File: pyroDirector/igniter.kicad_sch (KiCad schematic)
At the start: 13 parts, among them J28 LED_ext, J29 Screw_Terminal_01x02, K3 PR12-5V-360-1C, Q12 MMBT2222A 1P, Q13 IRLB8721PbF

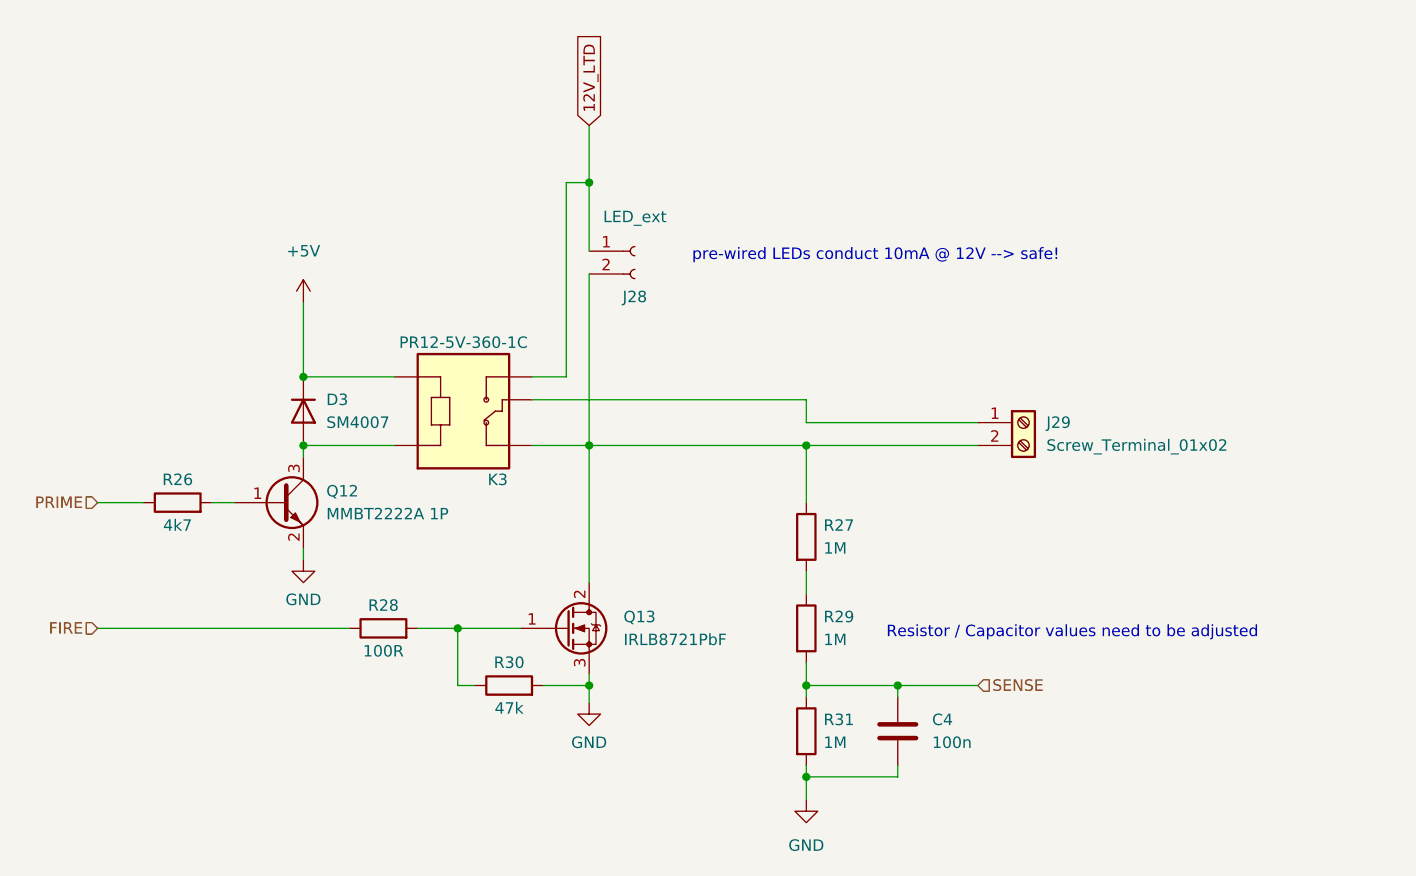
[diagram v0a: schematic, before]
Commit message: Added jacks and PCB switch
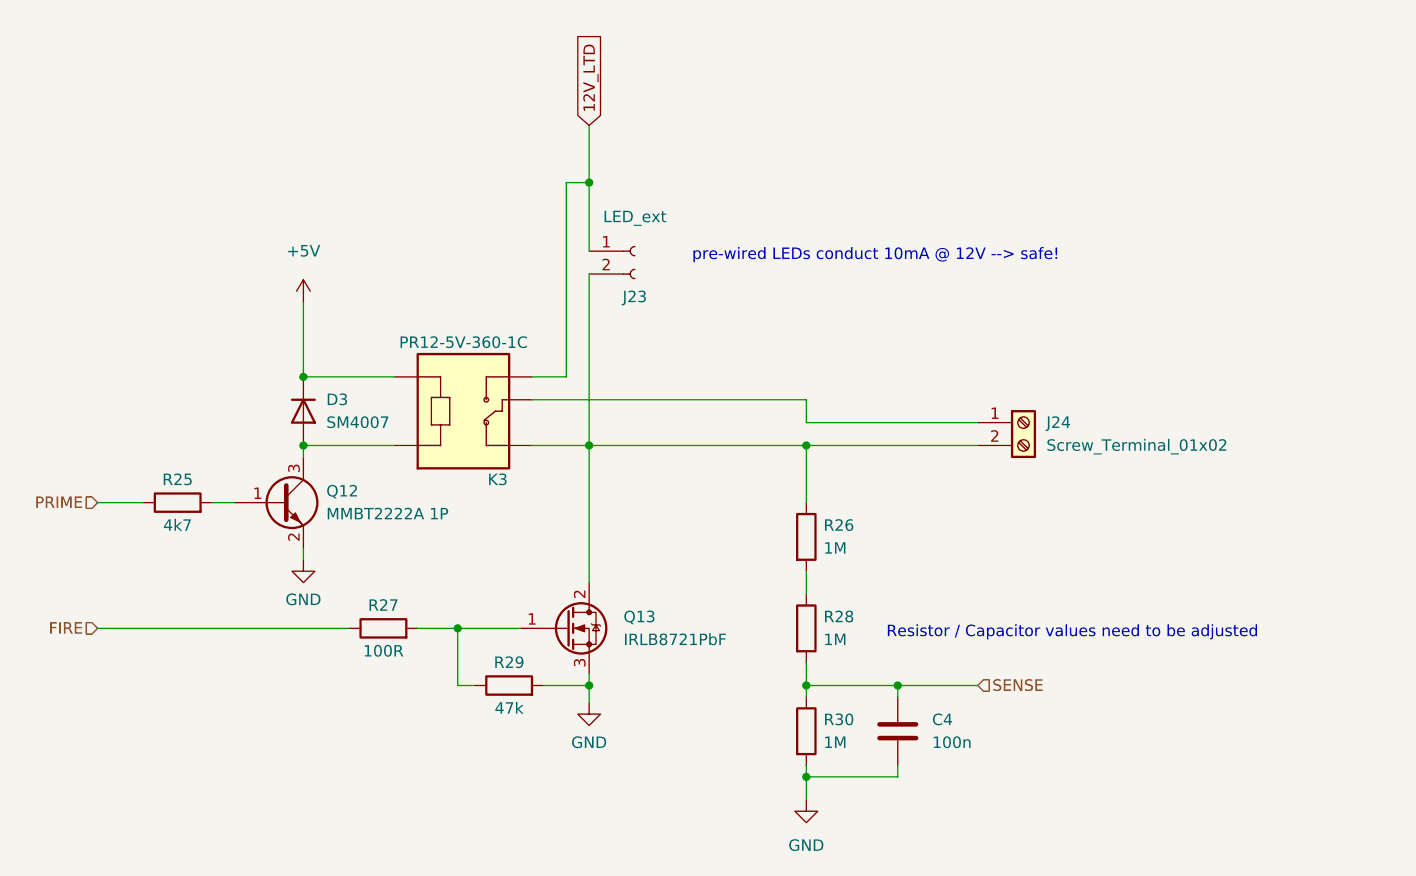
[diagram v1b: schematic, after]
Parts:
- C4: footprint (none) -> Capacitor_SMD:C_0805_2012Metric_Pad1.18x1.45mm_HandSolder
- renumbered J28 to J23, J29 to J24, R26 to R25, R27 to R26, R28 to R27, R29 to R28, R30 to R29, R31 to R30
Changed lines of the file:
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@@
   (symbol (lib_id "power:GND") (at 156.21 130.175 0) (unit 1)
     (in_bom yes) (on_board yes) (fields_autoplaced)
-    (property "Reference" "#PWR043" (id 0) (at 156.21 136.525 0)
+    (property "Reference" "#PWR049" (id 0) (at 156.21 136.525 0)
       (effects (font (size 1.27 1.27)) hide)
     )
@@
   (symbol (lib_id "Device:R") (at 110.49 107.95 90) (unit 1)
     (in_bom yes) (on_board yes)
-    (property "Reference" "R26" (id 0) (at 110.49 105.41 90))
+    (property "Reference" "R25" (id 0) (at 110.49 105.41 90))
     (property "Value" "4k7" (id 1) (at 110.49 110.49 90))
     (property "Footprint" "" (id 2) (at 110.49 109.728 90)
@@
   (symbol (lib_id "Connector:Conn_01x02_Female") (at 161.29 80.01 0) (unit 1)
     (in_bom yes) (on_board yes)
-    (property "Reference" "J28" (id 0) (at 161.29 85.09 0))
+    (property "Reference" "J23" (id 0) (at 161.29 85.09 0))
     (property "Value" "LED_ext" (id 1) (at 161.29 76.2 0))
     (property "Footprint" "" (id 2) (at 161.29 80.01 0)
@@
   (symbol (lib_id "power:GND") (at 180.34 140.97 0) (unit 1)
     (in_bom yes) (on_board yes) (fields_autoplaced)
-    (property "Reference" "#PWR044" (id 0) (at 180.34 147.32 0)
+    (property "Reference" "#PWR050" (id 0) (at 180.34 147.32 0)
       (effects (font (size 1.27 1.27)) hide)
     )
@@
   (symbol (lib_id "Device:R") (at 147.32 128.27 90) (unit 1)
     (in_bom yes) (on_board yes)
-    (property "Reference" "R30" (id 0) (at 147.32 125.73 90))
+    (property "Reference" "R29" (id 0) (at 147.32 125.73 90))
     (property "Value" "47k" (id 1) (at 147.32 130.81 90))
     (property "Footprint" "" (id 2) (at 147.32 130.048 90)
@@
   (symbol (lib_id "power:+5V") (at 124.46 85.725 0) (unit 1)
     (in_bom yes) (on_board yes) (fields_autoplaced)
-    (property "Reference" "#PWR041" (id 0) (at 124.46 89.535 0)
+    (property "Reference" "#PWR047" (id 0) (at 124.46 89.535 0)
       (effects (font (size 1.27 1.27)) hide)
     )
@@
   (symbol (lib_id "Device:R") (at 180.34 121.92 0) (unit 1)
     (in_bom yes) (on_board yes) (fields_autoplaced)
-    (property "Reference" "R29" (id 0) (at 182.245 120.6499 0)
+    (property "Reference" "R28" (id 0) (at 182.245 120.6499 0)
       (effects (font (size 1.27 1.27)) (justify left))
     )
@@
   (symbol (lib_id "Device:R") (at 180.34 133.35 0) (unit 1)
     (in_bom yes) (on_board yes) (fields_autoplaced)
-    (property "Reference" "R31" (id 0) (at 182.245 132.0799 0)
+    (property "Reference" "R30" (id 0) (at 182.245 132.0799 0)
       (effects (font (size 1.27 1.27)) (justify left))
     )
@@
   (symbol (lib_id "Device:R") (at 133.35 121.92 90) (unit 1)
     (in_bom yes) (on_board yes)
-    (property "Reference" "R28" (id 0) (at 133.35 119.38 90))
+    (property "Reference" "R27" (id 0) (at 133.35 119.38 90))
     (property "Value" "100R" (id 1) (at 133.35 124.46 90))
     (property "Footprint" "" (id 2) (at 133.35 123.698 90)
@@
   (symbol (lib_id "Connector:Screw_Terminal_01x02") (at 204.47 99.06 0) (unit 1)
     (in_bom yes) (on_board yes) (fields_autoplaced)
-    (property "Reference" "J29" (id 0) (at 207.01 99.0599 0)
+    (property "Reference" "J24" (id 0) (at 207.01 99.0599 0)
       (effects (font (size 1.27 1.27)) (justify left))
     )
@@
   (symbol (lib_id "power:GND") (at 124.46 114.3 0) (unit 1)
     (in_bom yes) (on_board yes) (fields_autoplaced)
-    (property "Reference" "#PWR042" (id 0) (at 124.46 120.65 0)
+    (property "Reference" "#PWR048" (id 0) (at 124.46 120.65 0)
       (effects (font (size 1.27 1.27)) hide)
     )
@@
       (effects (font (size 1.27 1.27)) (justify left))
     )
-    (property "Footprint" "" (id 2) (at 191.4652 137.16 0)
+    (property "Footprint" "Capacitor_SMD:C_0805_2012Metric_Pad1.18x1.45mm_HandSolder" (id 2) (at 191.4652 137.16 0)
       (effects (font (size 1.27 1.27)) hide)
     )
@@
   (symbol (lib_id "Device:R") (at 180.34 111.76 0) (unit 1)
     (in_bom yes) (on_board yes) (fields_autoplaced)
-    (property "Reference" "R27" (id 0) (at 182.245 110.4899 0)
-      (effects (font (size 1.27 1.27)) (justify left))
-    )
+    (property "Reference" "R26" (id 0) (at 182.245 110.4899 0)
+      (effects (font (size 1.27 1.27)) (justify left))
+    )

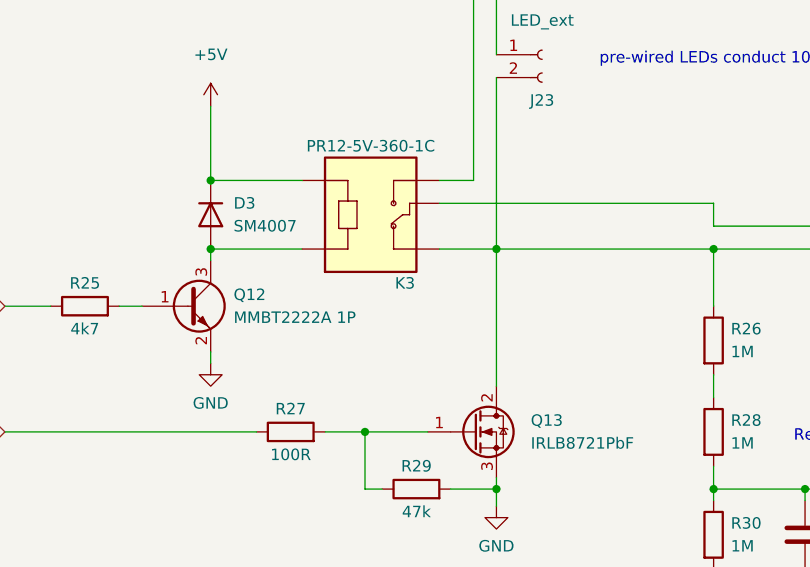
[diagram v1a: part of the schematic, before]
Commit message: first component placement, trigger header is missing!
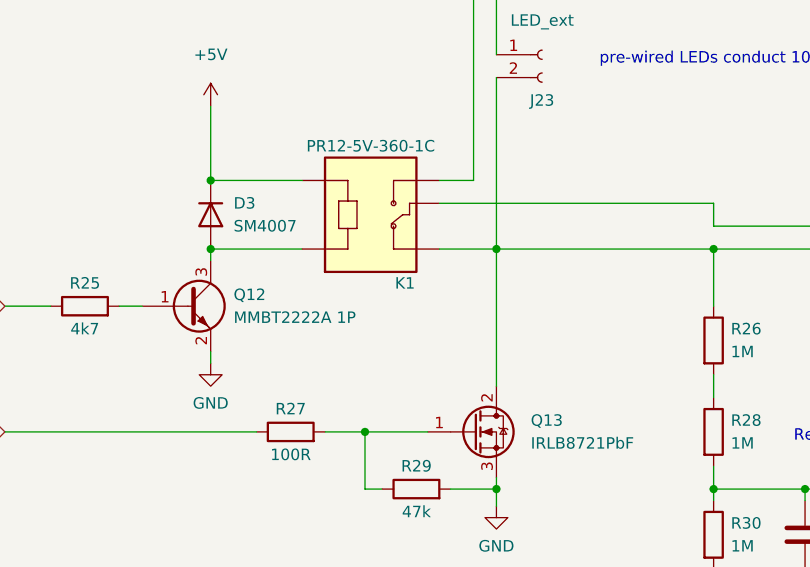
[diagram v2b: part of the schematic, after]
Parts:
- D3: footprint Diode_SMD:D_MELF -> Diode_SMD:D_SMA
- J23: footprint (none) -> Connector_PinHeader_2.54mm:PinHeader_1x02_P2.54mm_Vertical
- J24: footprint (none) -> TerminalBlock_Phoenix:TerminalBlock_Phoenix_PT-1,5-2-5.0-H_1x02_P5.00mm_Horizontal
- R25, R26, R27, R28, R29, R30: footprint (none) -> Resistor_SMD:R_0805_2012Metric_Pad1.20x1.40mm_HandSolder
- renumbered K3 to K1
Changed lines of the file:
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@@
     (property "Reference" "R25" (id 0) (at 110.49 105.41 90))
     (property "Value" "4k7" (id 1) (at 110.49 110.49 90))
-    (property "Footprint" "" (id 2) (at 110.49 109.728 90)
+    (property "Footprint" "Resistor_SMD:R_0805_2012Metric_Pad1.20x1.40mm_HandSolder" (id 2) (at 110.49 109.728 90)
       (effects (font (size 1.27 1.27)) hide)
     )
@@
     (property "Reference" "J23" (id 0) (at 161.29 85.09 0))
     (property "Value" "LED_ext" (id 1) (at 161.29 76.2 0))
-    (property "Footprint" "" (id 2) (at 161.29 80.01 0)
+    (property "Footprint" "Connector_PinHeader_2.54mm:PinHeader_1x02_P2.54mm_Vertical" (id 2) (at 161.29 80.01 0)
       (effects (font (size 1.27 1.27)) hide)
     )
@@
     (property "Reference" "R29" (id 0) (at 147.32 125.73 90))
     (property "Value" "47k" (id 1) (at 147.32 130.81 90))
-    (property "Footprint" "" (id 2) (at 147.32 130.048 90)
+    (property "Footprint" "Resistor_SMD:R_0805_2012Metric_Pad1.20x1.40mm_HandSolder" (id 2) (at 147.32 130.048 90)
       (effects (font (size 1.27 1.27)) hide)
     )
@@
   (symbol (lib_id "CUI Relays:PR12-5V-360-1C") (at 142.24 96.52 0) (unit 1)
     (in_bom yes) (on_board yes)
-    (property "Reference" "K3" (id 0) (at 146.05 105.41 0))
+    (property "Reference" "K1" (id 0) (at 146.05 105.41 0))
     (property "Value" "PR12-5V-360-1C" (id 1) (at 142.24 90.17 0))
     (property "Footprint" "CUI Relays:PR12-5V-360-1C" (id 2) (at 142.24 90.17 0)
@@
       (effects (font (size 1.27 1.27)) (justify left))
     )
-    (property "Footprint" "" (id 2) (at 178.562 121.92 90)
+    (property "Footprint" "Resistor_SMD:R_0805_2012Metric_Pad1.20x1.40mm_HandSolder" (id 2) (at 178.562 121.92 90)
       (effects (font (size 1.27 1.27)) hide)
     )
@@
       (effects (font (size 1.27 1.27)) (justify left))
     )
-    (property "Footprint" "" (id 2) (at 178.562 133.35 90)
+    (property "Footprint" "Resistor_SMD:R_0805_2012Metric_Pad1.20x1.40mm_HandSolder" (id 2) (at 178.562 133.35 90)
       (effects (font (size 1.27 1.27)) hide)
     )
@@
     (property "Reference" "R27" (id 0) (at 133.35 119.38 90))
     (property "Value" "100R" (id 1) (at 133.35 124.46 90))
-    (property "Footprint" "" (id 2) (at 133.35 123.698 90)
+    (property "Footprint" "Resistor_SMD:R_0805_2012Metric_Pad1.20x1.40mm_HandSolder" (id 2) (at 133.35 123.698 90)
       (effects (font (size 1.27 1.27)) hide)
     )
@@
       (effects (font (size 1.27 1.27)) (justify left))
     )
-    (property "Footprint" "" (id 2) (at 204.47 99.06 0)
+    (property "Footprint" "TerminalBlock_Phoenix:TerminalBlock_Phoenix_PT-1,5-2-5.0-H_1x02_P5.00mm_Horizontal" (id 2) (at 204.47 99.06 0)
       (effects (font (size 1.27 1.27)) hide)
     )
@@
       (effects (font (size 1.27 1.27)) (justify left))
     )
-    (property "Footprint" "" (id 2) (at 178.562 111.76 90)
+    (property "Footprint" "Resistor_SMD:R_0805_2012Metric_Pad1.20x1.40mm_HandSolder" (id 2) (at 178.562 111.76 90)
       (effects (font (size 1.27 1.27)) hide)
     )
@@
       (effects (font (size 1.27 1.27)) (justify left))
     )
-    (property "Footprint" "Diode_SMD:D_MELF" (id 2) (at 120.015 97.79 0)
-      (effects (font (size 1.27 1.27)) hide)
-    )
+    (property "Footprint" "Diode_SMD:D_SMA" (id 2) (at 120.015 97.79 0)
+      (effects (font (size 1.27 1.27)) hide)
+    )

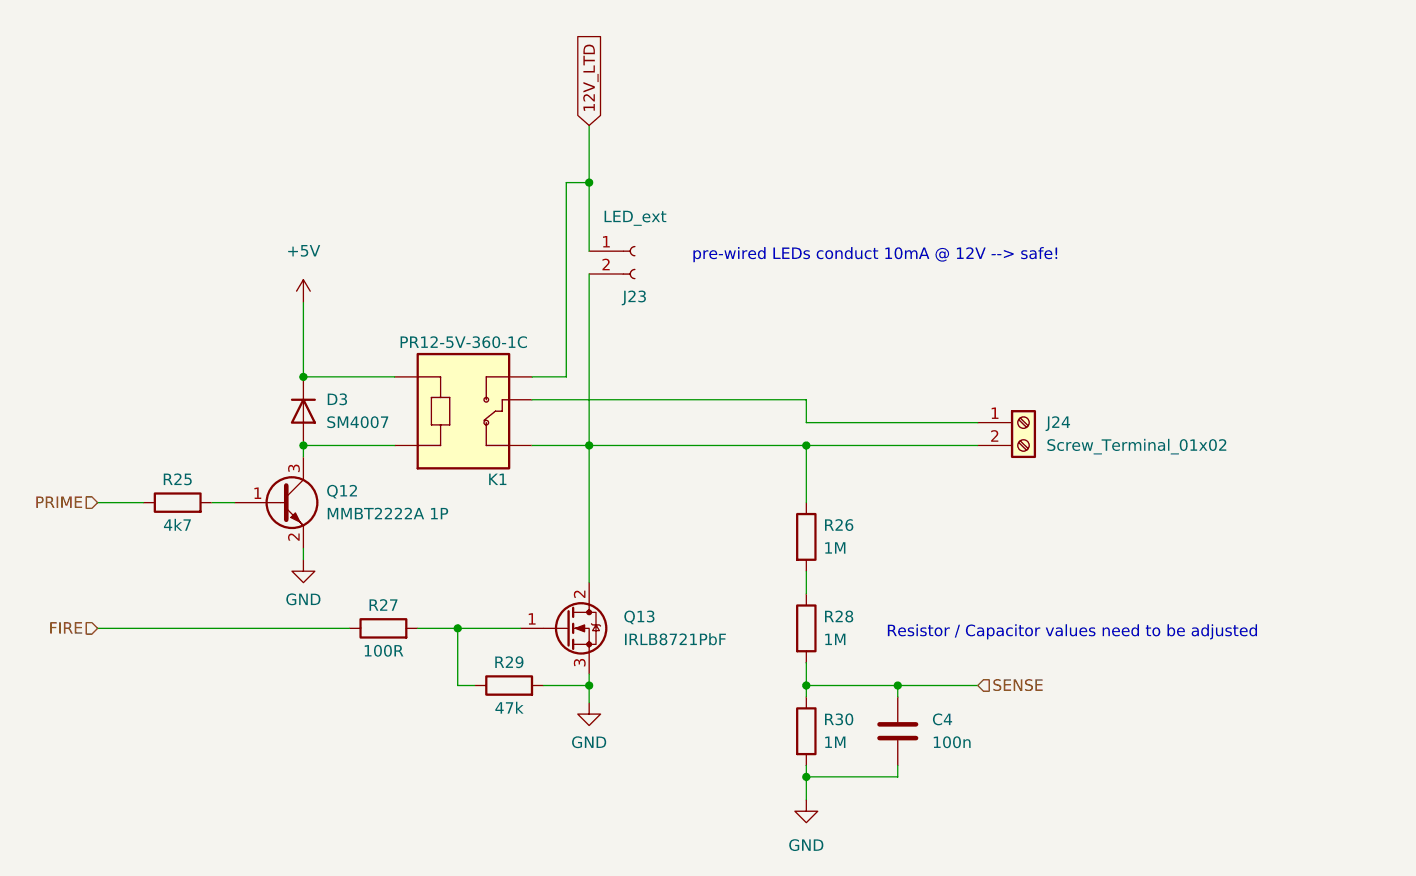
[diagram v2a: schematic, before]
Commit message: placement improvements, added missing header -->should we use handsolder pads?
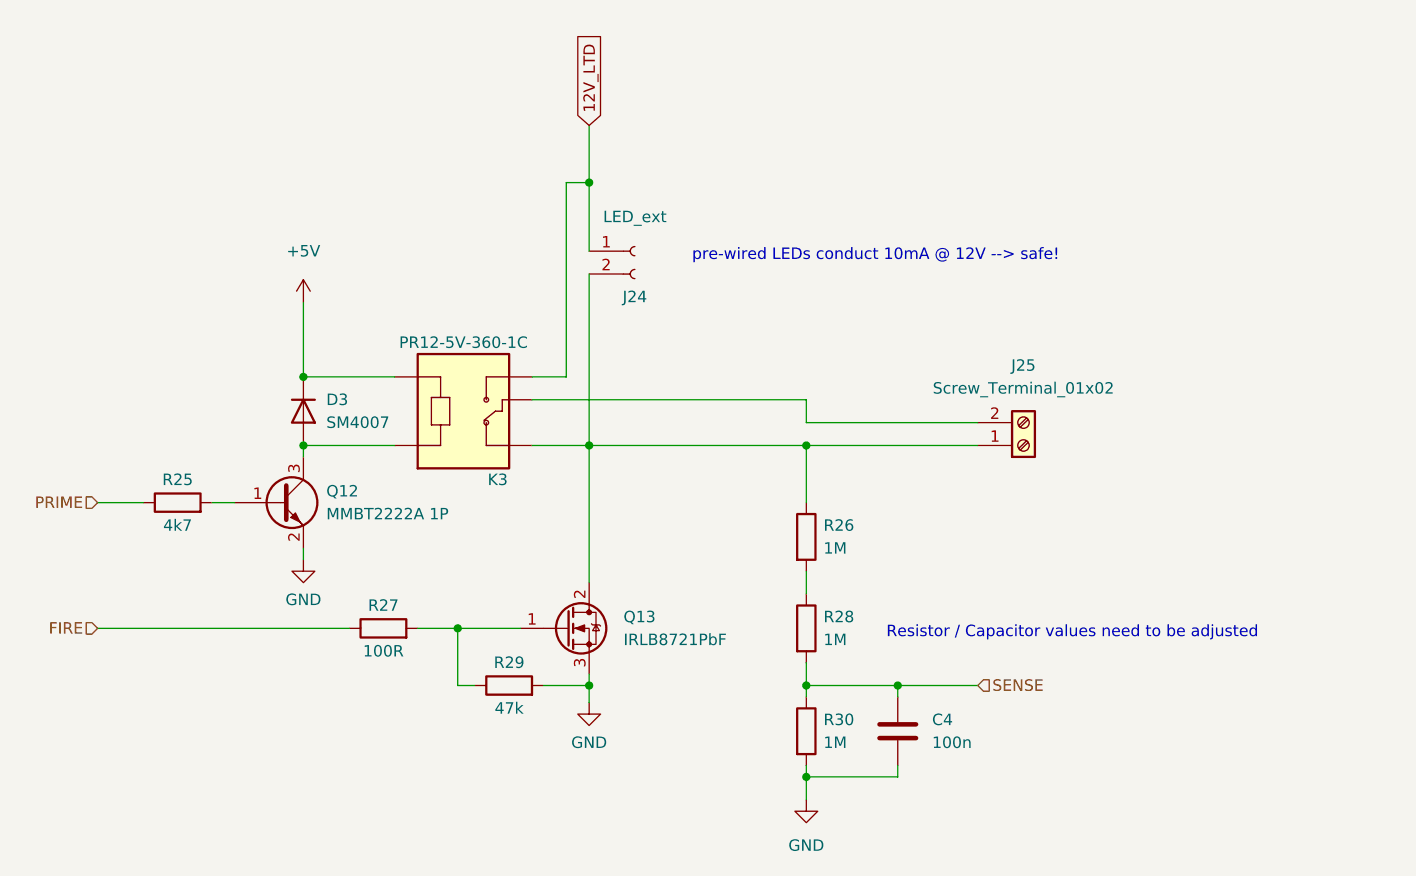
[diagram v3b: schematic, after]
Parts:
- renumbered J23 to J24, J24 to J25, K1 to K3
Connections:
- net at J24.2 (Pin_2), K3.NC, Q13.2 (D)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: now also J25.1 (Pin_1); no longer J25.2 (Pin_2)
- net at K3.COM: now also J25.2 (Pin_2); no longer J25.1 (Pin_1)
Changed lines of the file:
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@@
   (symbol (lib_id "Connector:Conn_01x02_Female") (at 161.29 80.01 0) (unit 1)
     (in_bom yes) (on_board yes)
-    (property "Reference" "J23" (id 0) (at 161.29 85.09 0))
+    (property "Reference" "J24" (id 0) (at 161.29 85.09 0))
     (property "Value" "LED_ext" (id 1) (at 161.29 76.2 0))
     (property "Footprint" "Connector_PinHeader_2.54mm:PinHeader_1x02_P2.54mm_Vertical" (id 2) (at 161.29 80.01 0)
@@
   (symbol (lib_id "CUI Relays:PR12-5V-360-1C") (at 142.24 96.52 0) (unit 1)
     (in_bom yes) (on_board yes)
-    (property "Reference" "K1" (id 0) (at 146.05 105.41 0))
+    (property "Reference" "K3" (id 0) (at 146.05 105.41 0))
     (property "Value" "PR12-5V-360-1C" (id 1) (at 142.24 90.17 0))
     (property "Footprint" "CUI Relays:PR12-5V-360-1C" (id 2) (at 142.24 90.17 0)
@@
     (pin "2")
   )
-  (symbol (lib_id "Connector:Screw_Terminal_01x02") (at 204.47 99.06 0) (unit 1)
+  (symbol (lib_id "Connector:Screw_Terminal_01x02") (at 204.47 101.6 0) (mirror x) (unit 1)
     (in_bom yes) (on_board yes) (fields_autoplaced)
-    (property "Reference" "J24" (id 0) (at 207.01 99.0599 0)
-      (effects (font (size 1.27 1.27)) (justify left))
-    )
-    (property "Value" "Screw_Terminal_01x02" (id 1) (at 207.01 101.5999 0)
-      (effects (font (size 1.27 1.27)) (justify left))
-    )
-    (property "Footprint" "TerminalBlock_Phoenix:TerminalBlock_Phoenix_PT-1,5-2-5.0-H_1x02_P5.00mm_Horizontal" (id 2) (at 204.47 99.06 0)
+    (property "Reference" "J25" (id 0) (at 204.47 92.71 0))
+    (property "Value" "Screw_Terminal_01x02" (id 1) (at 204.47 95.25 0))
+    (property "Footprint" "TerminalBlock_Phoenix:TerminalBlock_Phoenix_PT-1,5-2-5.0-H_1x02_P5.00mm_Horizontal" (id 2) (at 204.47 101.6 0)
       (effects (font (size 1.27 1.27)) hide)
     )
-    (property "Datasheet" "~" (id 3) (at 204.47 99.06 0)
+    (property "Datasheet" "~" (id 3) (at 204.47 101.6 0)
       (effects (font (size 1.27 1.27)) hide)
     )
